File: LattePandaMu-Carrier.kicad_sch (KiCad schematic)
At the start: 6 parts

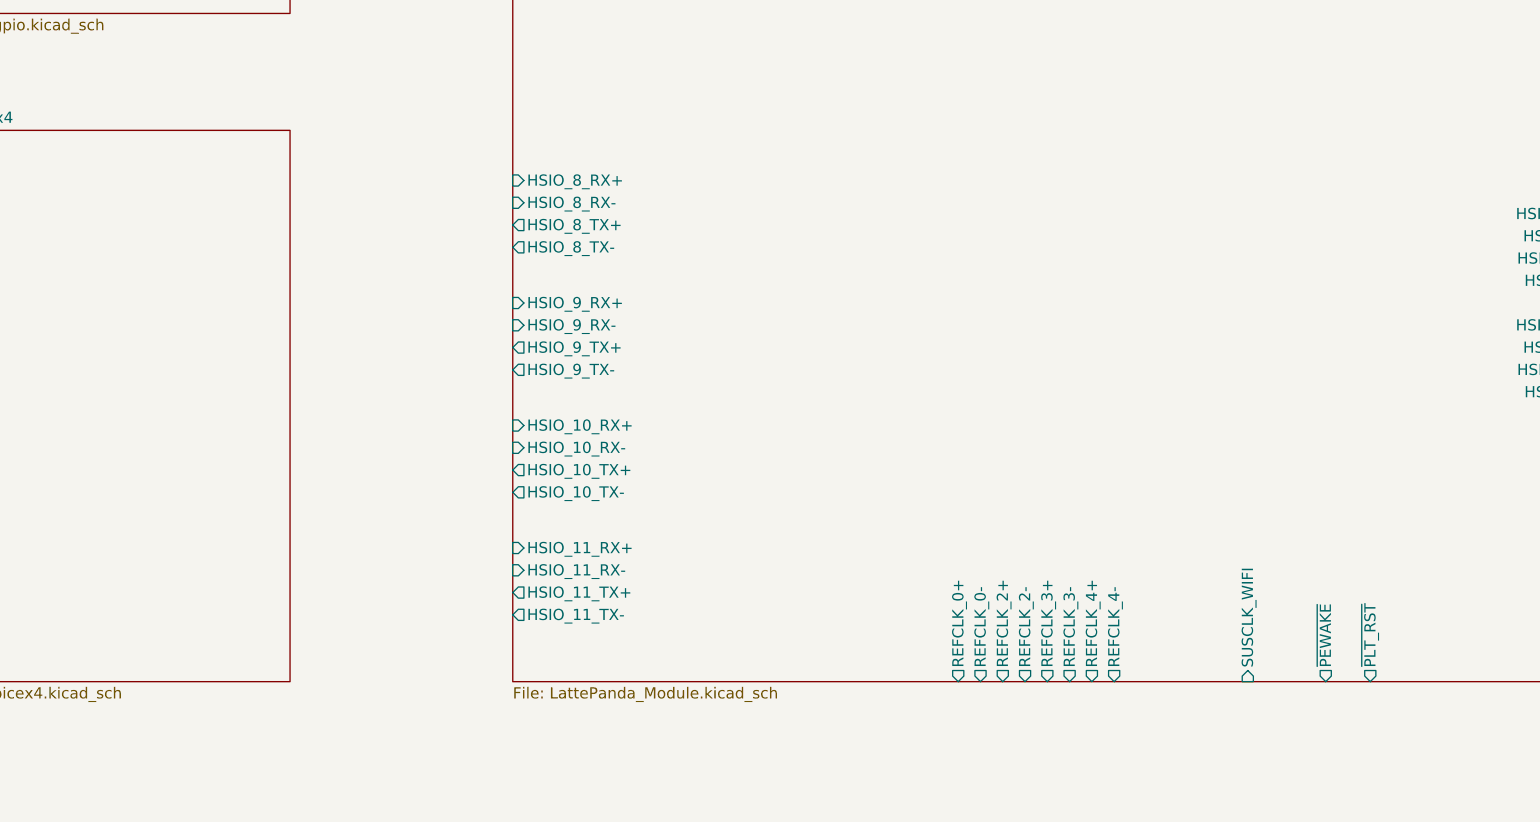
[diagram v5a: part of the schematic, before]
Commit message: feat(pcie): Added PCIe x4 implementation and connections.
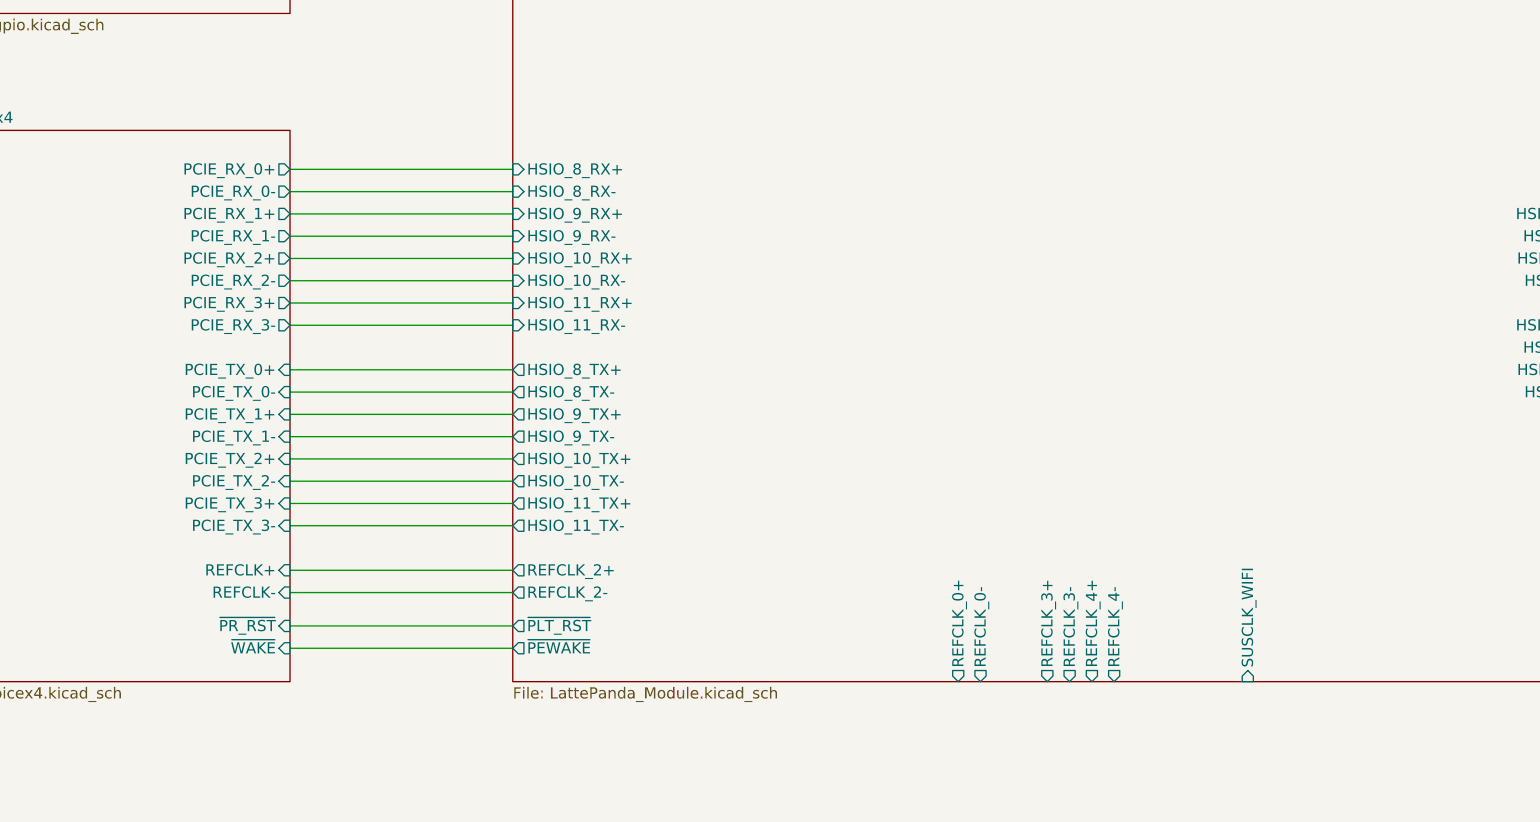
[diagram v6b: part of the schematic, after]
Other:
- sheet PCIe x4 ports: added PCIE_RX_0+, PCIE_RX_0-, PCIE_RX_1+, PCIE_RX_1-, PCIE_RX_2+, PCIE_RX_2-, PCIE_RX_3+, PCIE_RX_3-, PCIE_TX_0+, PCIE_TX_0-, PCIE_TX_1+, PCIE_TX_1-, PCIE_TX_2+, PCIE_TX_2-, PCIE_TX_3+, PCIE_TX_3-, REFCLK+, REFCLK-, ~{PR_RST}, ~{WAKE}; removed none

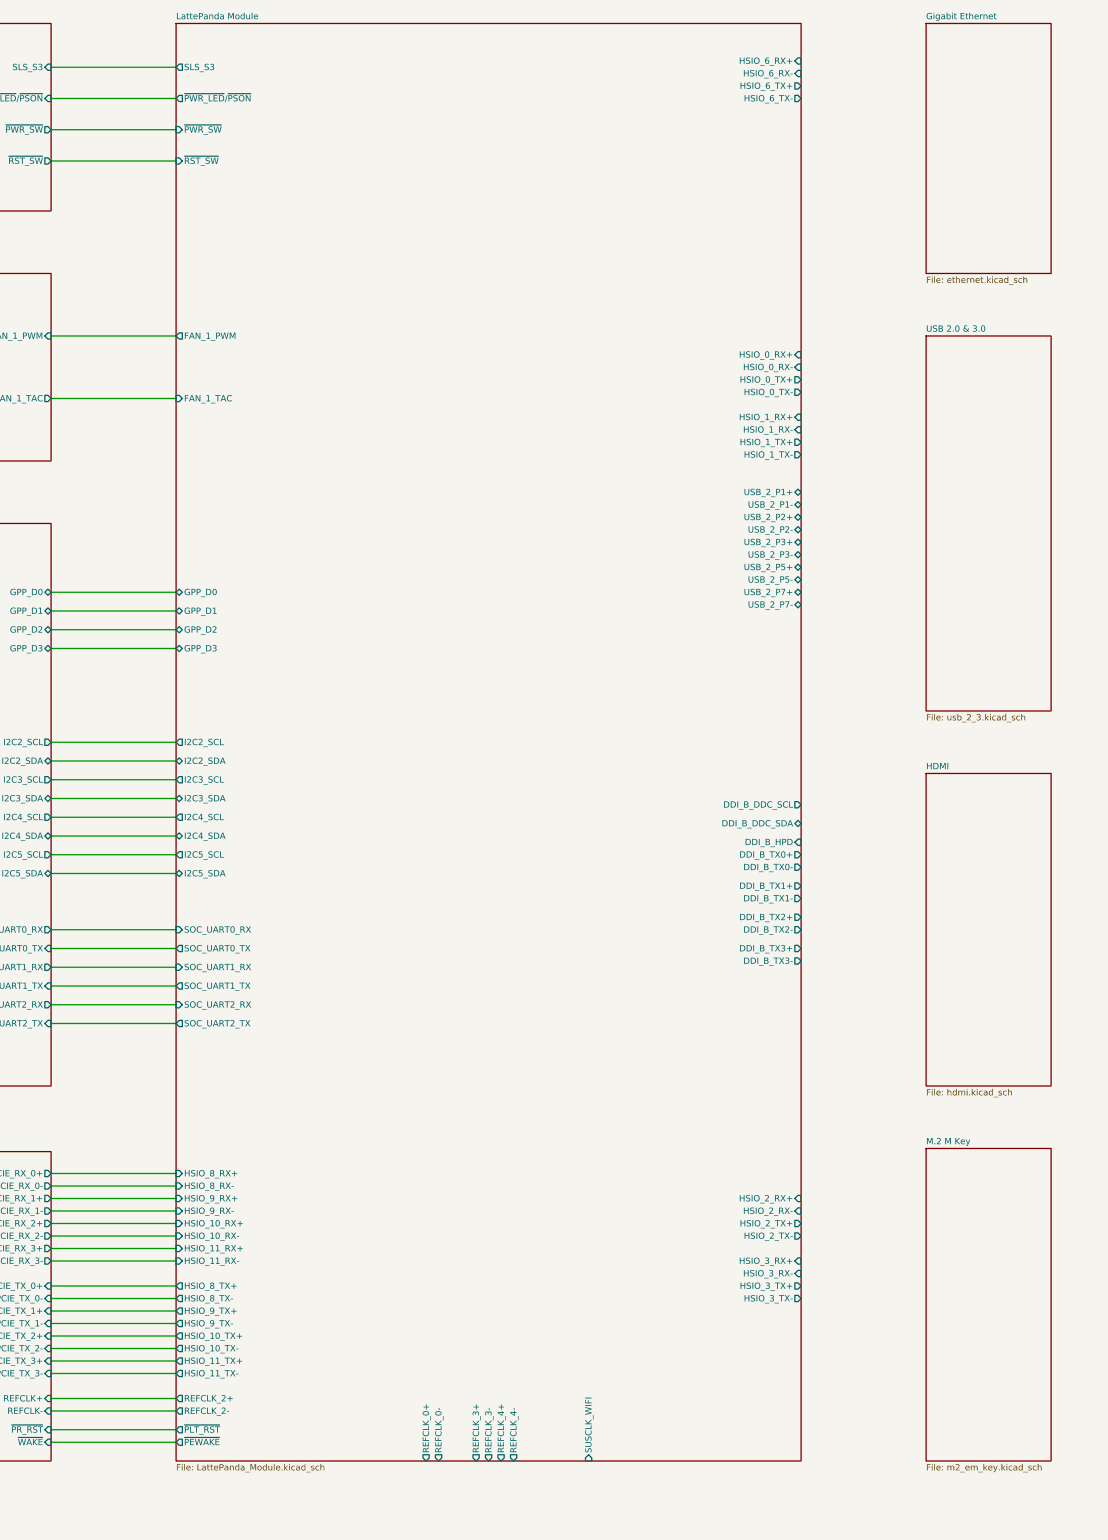
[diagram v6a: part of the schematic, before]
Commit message: feat(ethernet): Added Gigabit Ethernet implementation and connections.
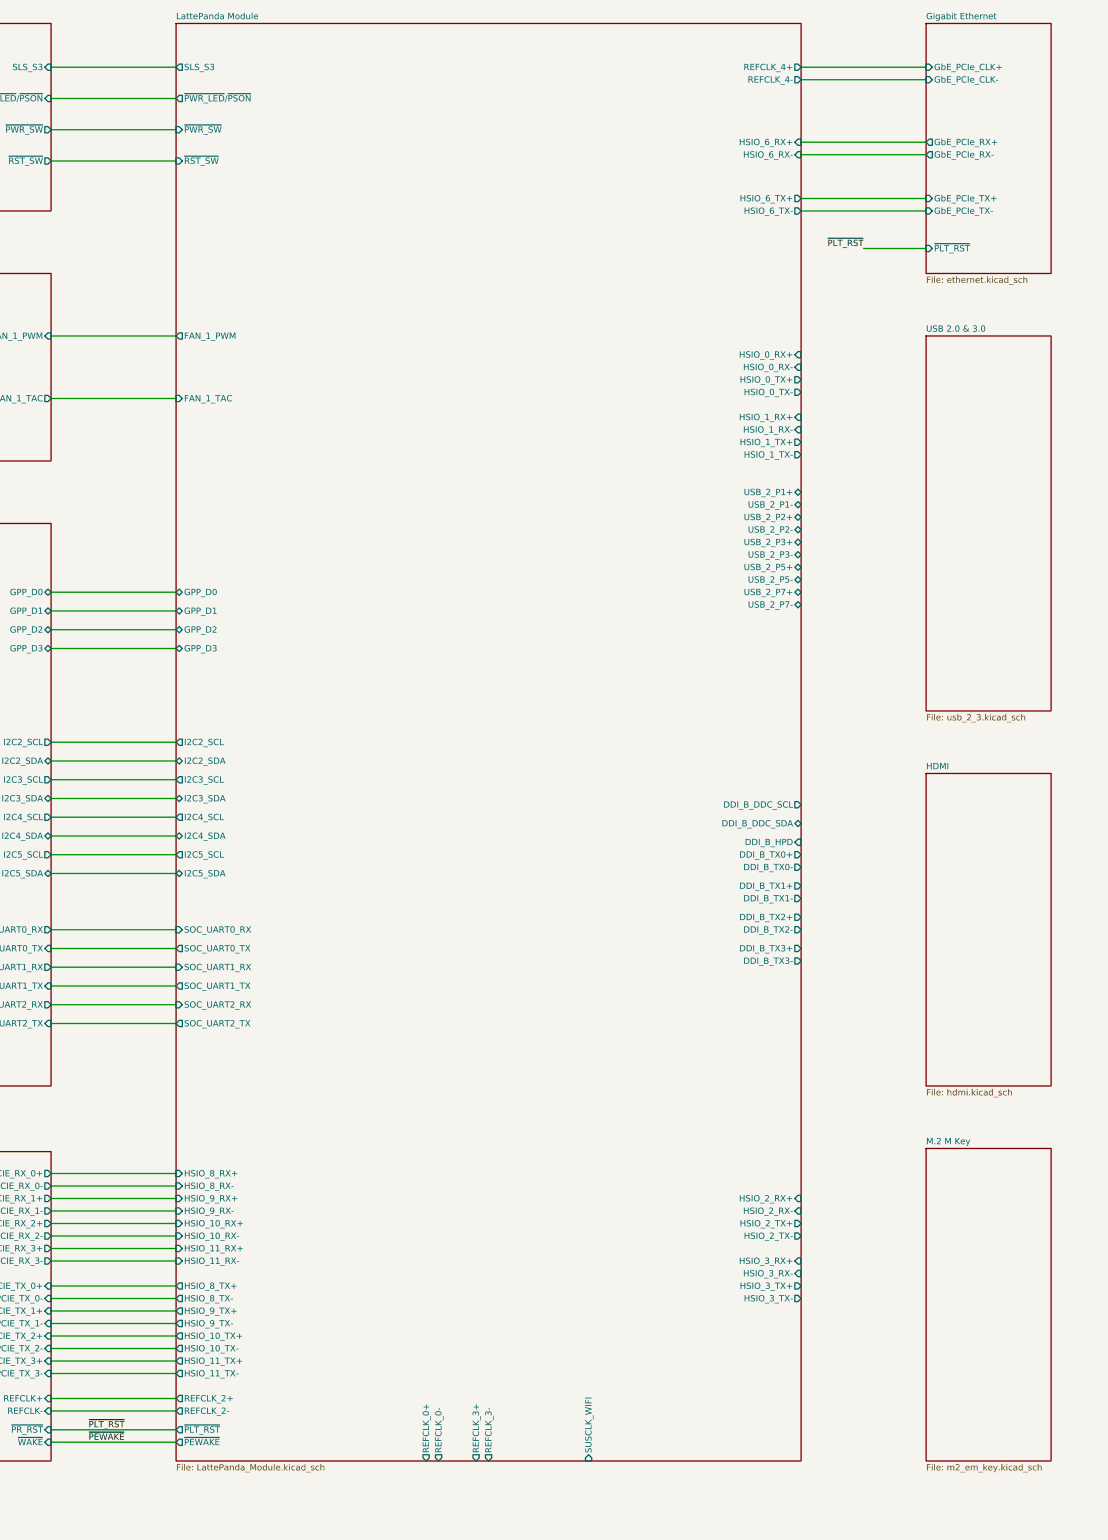
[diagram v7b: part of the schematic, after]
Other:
- sheet Gigabit Ethernet ports: added GbE_PCIe_CLK+, GbE_PCIe_CLK-, GbE_PCIe_RX+, GbE_PCIe_RX-, GbE_PCIe_TX+, GbE_PCIe_TX-, ~{PLT_RST}; removed none
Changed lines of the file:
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@@
+	(wire
+		(pts
+			(xy 330.2 96.52) (xy 342.9 96.52)
+		)
+		(stroke
+			(width 0)
+			(type default)
+		)
+	)
 	(wire
 		(pts
@@
 	(wire
 		(pts
+			(xy 317.5 62.23) (xy 342.9 62.23)
+		)
+		(stroke
+			(width 0)
+			(type default)
+		)
+	)
+	(wire
+		(pts
 			(xy 165.1 208.28) (xy 190.5 208.28)
+		)
+		(stroke
+			(width 0)
+			(type default)
+		)
+	)
+	(wire
+		(pts
+			(xy 317.5 74.93) (xy 342.9 74.93)
 		)
 		(stroke
@@
 	(wire
 		(pts
+			(xy 317.5 86.36) (xy 342.9 86.36)
+		)
+		(stroke
+			(width 0)
+			(type default)
+		)
+	)
+	(wire
+		(pts
+			(xy 317.5 88.9) (xy 342.9 88.9)
+		)
+		(stroke
+			(width 0)
+			(type default)
+		)
+	)
+	(wire
+		(pts
 			(xy 165.1 223.52) (xy 190.5 223.52)
 		)
@@
 	(wire
 		(pts
+			(xy 317.5 59.69) (xy 342.9 59.69)
+		)
+		(stroke
+			(width 0)
+			(type default)
+		)
+	)
+	(wire
+		(pts
 			(xy 165.1 166.37) (xy 190.5 166.37)
 		)
@@
 	(wire
 		(pts
+			(xy 317.5 77.47) (xy 342.9 77.47)
+		)
+		(stroke
+			(width 0)
+			(type default)
+		)
+	)
+	(wire
+		(pts
 			(xy 165.1 320.04) (xy 190.5 320.04)
 		)
@@
 			(width 0)
 			(type default)
+		)
+	)
+	(label "~{PLT_RST}"
+		(at 330.2 96.52 180)
+		(effects
+			(font
+				(size 1.27 1.27)
+			)
+			(justify right bottom)
+		)
+	)
+	(label "~{PLT_RST}"
+		(at 172.72 336.55 0)
+		(effects
+			(font
+				(size 1.27 1.27)
+			)
+			(justify left bottom)
+		)
+	)
+	(label "~{PEWAKE}"
+		(at 172.72 339.09 0)
+		(effects
+			(font
+				(size 1.27 1.27)
+			)
+			(justify left bottom)
 		)
 	)
@@
 			)
 		)
+		(pin "GbE_PCIe_CLK+" input
+			(at 342.9 59.69 180)
+			(effects
+				(font
+					(size 1.27 1.27)
+				)
+				(justify left)
+			)
+		)
+		(pin "GbE_PCIe_CLK-" input
+			(at 342.9 62.23 180)
+			(effects
+				(font
+					(size 1.27 1.27)
+				)
+				(justify left)
+			)
+		)
+		(pin "GbE_PCIe_RX+" output
+			(at 342.9 74.93 180)
+			(effects
+				(font
+					(size 1.27 1.27)
+				)
+				(justify left)
+			)
+		)
+		(pin "GbE_PCIe_RX-" output
+			(at 342.9 77.47 180)
+			(effects
+				(font
+					(size 1.27 1.27)
+				)
+				(justify left)
+			)
+		)
+		(pin "GbE_PCIe_TX+" input
+			(at 342.9 86.36 180)
+			(effects
+				(font
+					(size 1.27 1.27)
+				)
+				(justify left)
+			)
+		)
+		(pin "GbE_PCIe_TX-" input
+			(at 342.9 88.9 180)
+			(effects
+				(font
+					(size 1.27 1.27)
+				)
+				(justify left)
+			)
+		)
+		(pin "~{PLT_RST}" input
+			(at 342.9 96.52 180)
+			(effects
+				(font
+					(size 1.27 1.27)
+				)
+				(justify left)
+			)
+		)
 		(instances
 			(project "LattePandaMu-Carrier"
@@
 		)
 		(pin "HSIO_6_RX+" input
-			(at 317.5 58.42 0)
+			(at 317.5 74.93 0)
 			(effects
 				(font
@@
 		)
 		(pin "HSIO_6_RX-" input
-			(at 317.5 60.96 0)
+			(at 317.5 77.47 0)
 			(effects
 				(font
@@
 		)
 		(pin "HSIO_6_TX+" output
-			(at 317.5 63.5 0)
+			(at 317.5 86.36 0)
 			(effects
 				(font
@@
 		)
 		(pin "HSIO_6_TX-" output
-			(at 317.5 66.04 0)
+			(at 317.5 88.9 0)
 			(effects
 				(font
@@
 		)
 		(pin "REFCLK_4+" output
-			(at 256.54 342.9 270)
-			(effects
-				(font
-					(size 1.27 1.27)
-				)
-				(justify left)
+			(at 317.5 59.69 0)
+			(effects
+				(font
+					(size 1.27 1.27)
+				)
+				(justify right)
 			)
 		)
 		(pin "REFCLK_4-" output
-			(at 259.08 342.9 270)
-			(effects
-				(font
-					(size 1.27 1.27)
-				)
-				(justify left)
-			)
-		)
+			(at 317.5 62.23 0)
+			(effects
+				(font
+					(size 1.27 1.27)
+				)
+				(justify right)
+			)
+		)

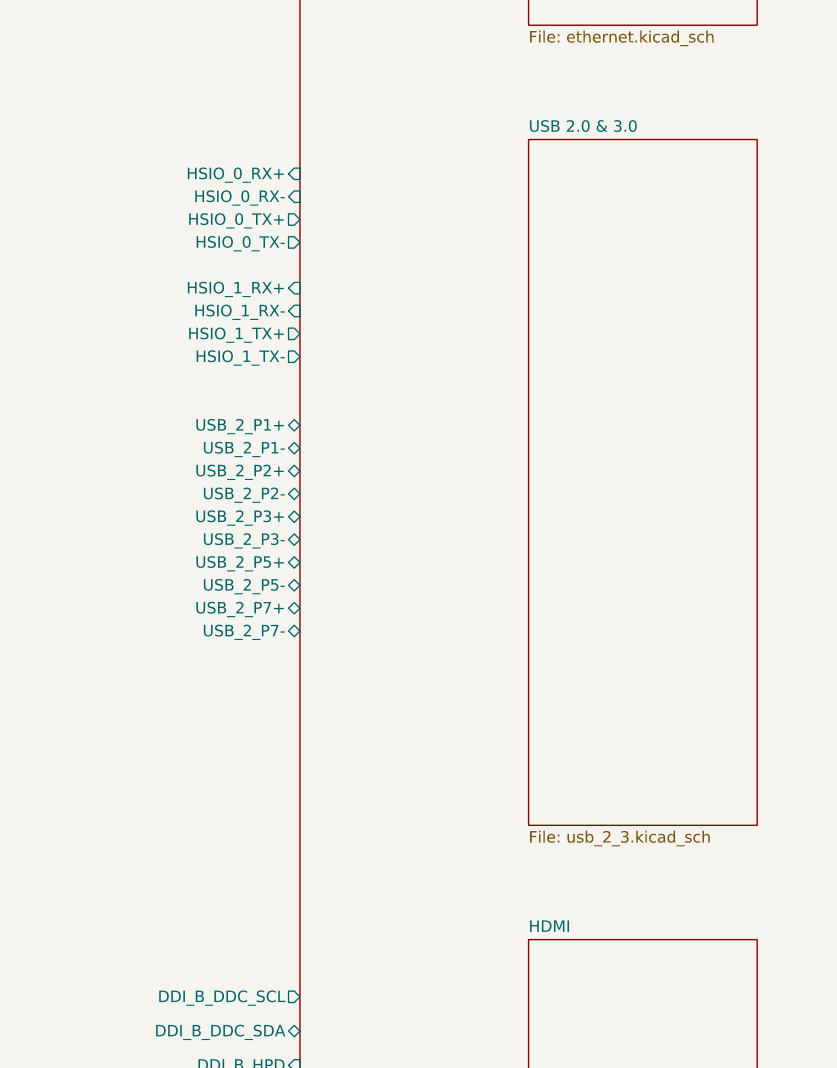
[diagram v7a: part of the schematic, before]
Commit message: feat(usb): Added usb 2.0 & usb 3.0 implementation and connections.
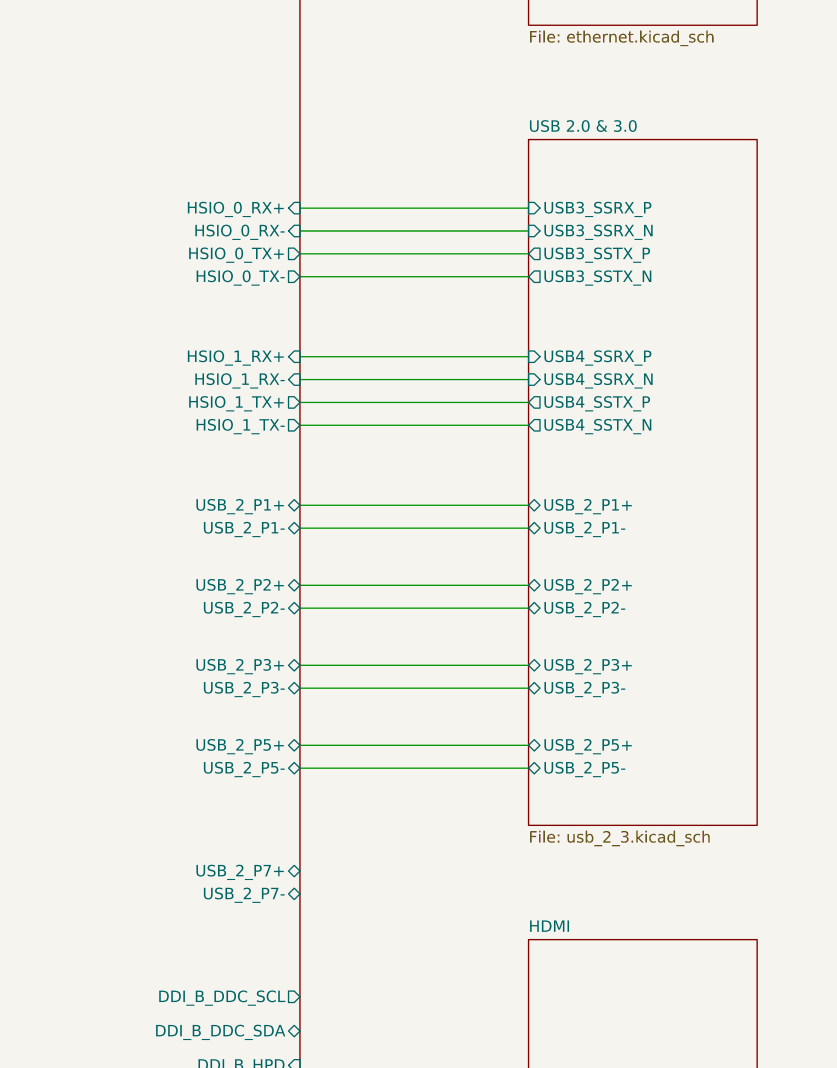
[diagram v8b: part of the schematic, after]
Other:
- sheet USB 2.0 & 3.0 ports: added USB3_SSRX_N, USB3_SSRX_P, USB3_SSTX_N, USB3_SSTX_P, USB4_SSRX_N, USB4_SSRX_P, USB4_SSTX_N, USB4_SSTX_P, USB_2_P1+, USB_2_P1-, USB_2_P2+, USB_2_P2-, USB_2_P3+, USB_2_P3-, USB_2_P5+, USB_2_P5-; removed none
